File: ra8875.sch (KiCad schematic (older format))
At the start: 6 parts

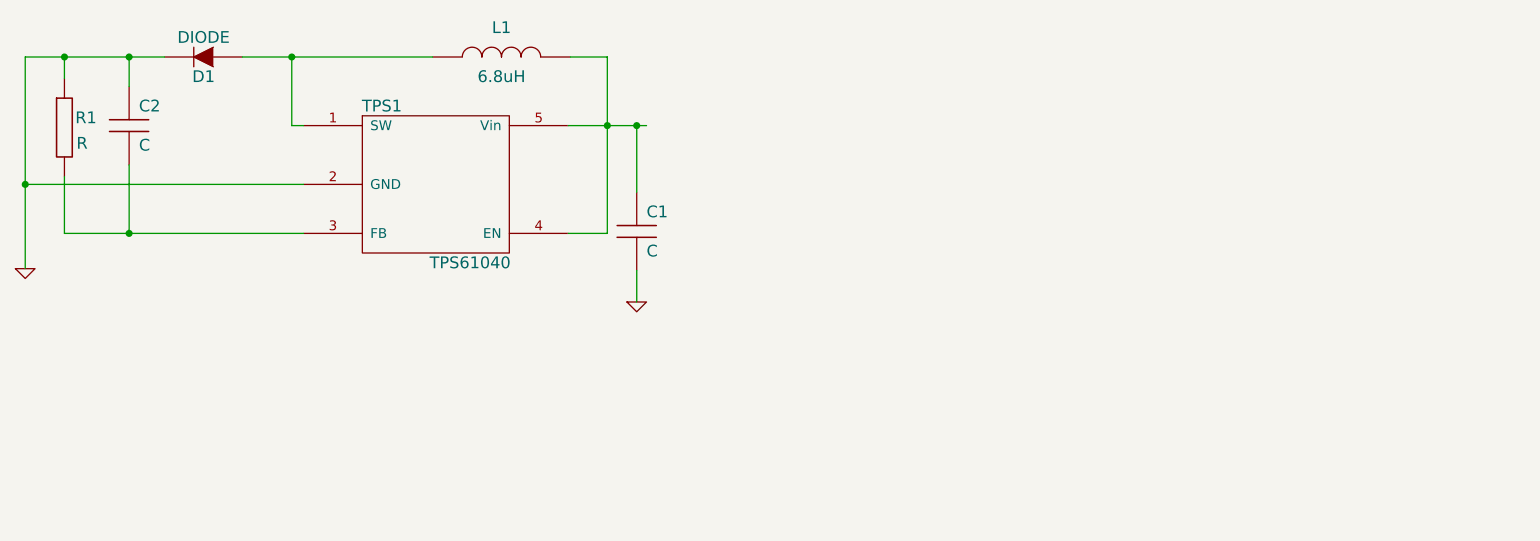
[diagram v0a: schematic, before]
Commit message: Add datasheets, appnotes and also completes the preliminary design for the TPS61040 power supply for the LCD backlight
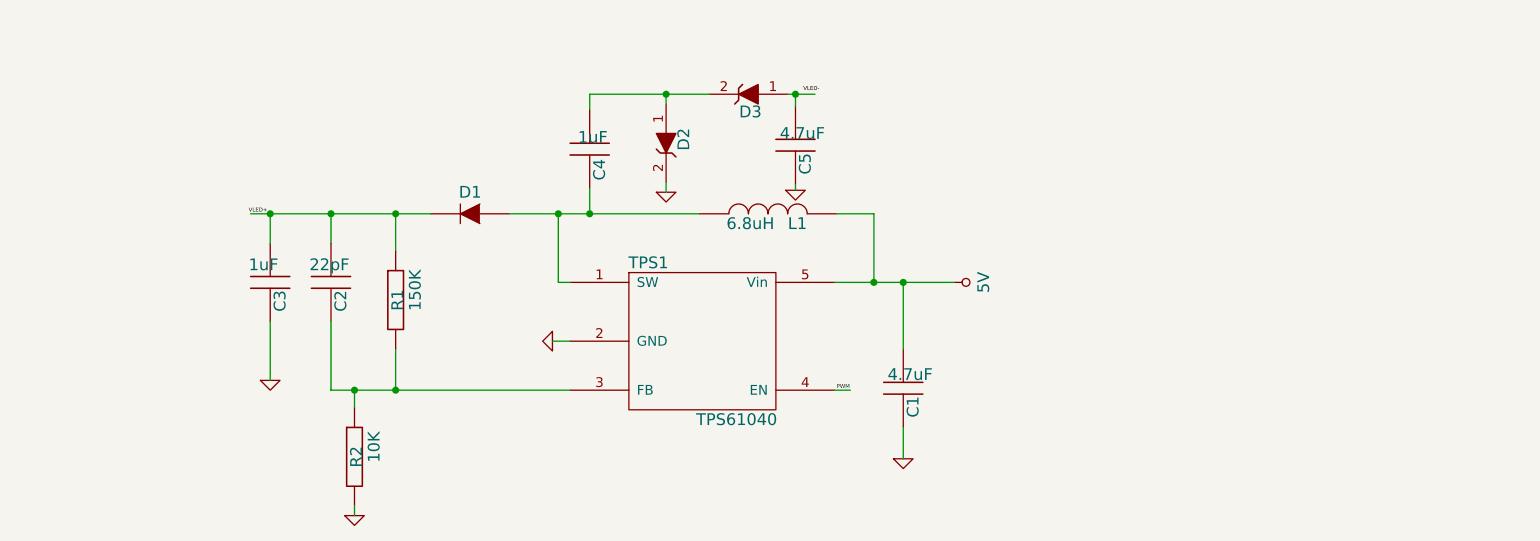
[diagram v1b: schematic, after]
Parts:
- added C3, C4: 1uF, symbol C
- added C5: 4.7uF, symbol C
- added D2, D3: ZENER, symbol ZENER
- added R2: 10K, symbol R
- C1: value C -> 4.7uF
- C2: value C -> 22pF
- R1: value R -> 150K
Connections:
- net labels added: 5V, PWM, VLED+, VLED-
- wire segments 18 -> 28
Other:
- moved on the sheet: C1, C2, D1, L1, R1, TPS1

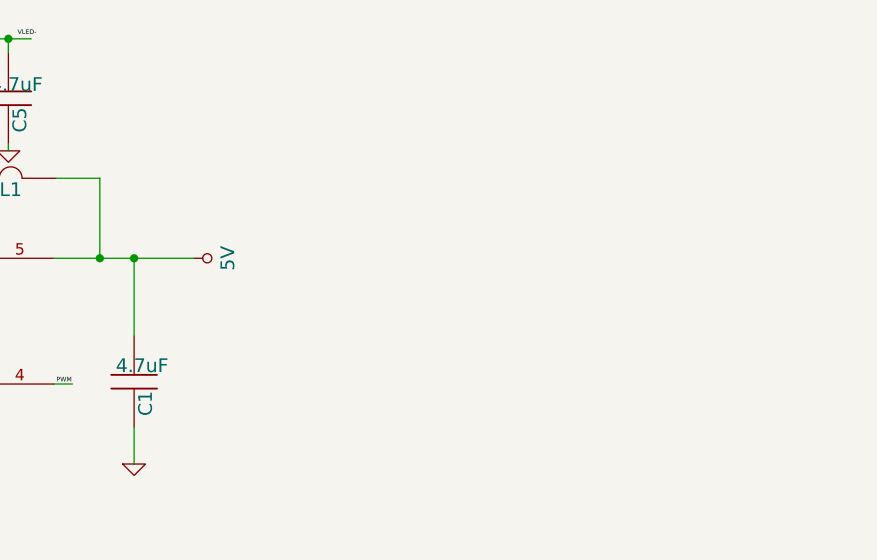
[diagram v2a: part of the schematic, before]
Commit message: Added Micrel 3.3v component
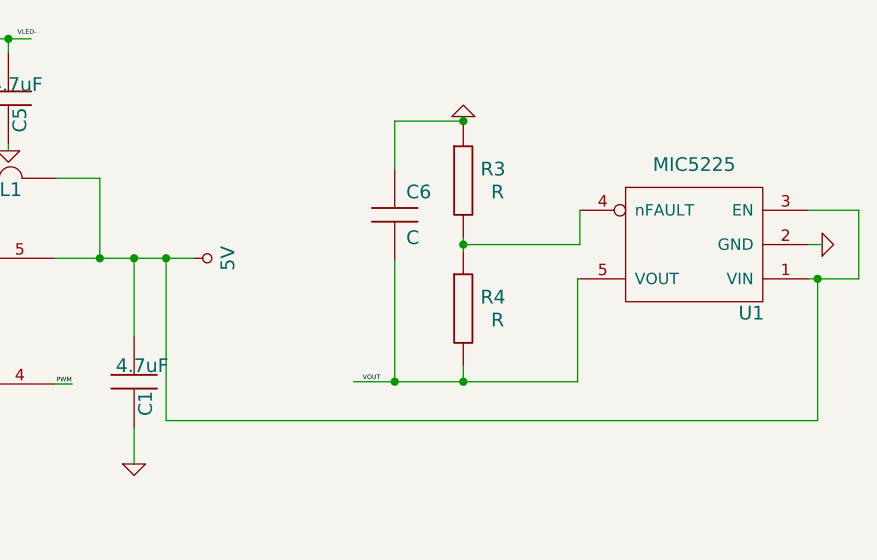
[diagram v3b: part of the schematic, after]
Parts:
- added C6: C, symbol C
- added R3, R4: R, symbol R
- added U1: MIC5225, symbol MIC2090-1YM5
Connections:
- net labels added: VOUT
- wire segments 28 -> 46
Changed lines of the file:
@@
 Sheet 1 1
 Title ""
-Date "7 may 2014"
+Date "20 may 2014"
 Rev ""
 Comp ""
@@
 	1    0    0    -1
 $EndComp
-Wire Wire Line
-	4980 2340 5590 2340
-Wire Wire Line
-	5330 2340 5330 2680
-Connection ~ 5330 2340
-Wire Wire Line
-	5330 3080 5330 3240
-Wire Wire Line
-	4990 1990 5180 1990
-Wire Wire Line
-	3320 1990 4290 1990
-Wire Wire Line
-	3630 2340 3570 2340
-Wire Wire Line
-	3570 2340 3570 1990
-Connection ~ 3570 1990
-Wire Wire Line
-	2000 1990 2920 1990
-Wire Wire Line
-	2410 2890 3630 2890
-Wire Wire Line
-	2740 1990 2740 2180
-Connection ~ 2740 1990
-Wire Wire Line
-	2410 2540 2410 2890
-Wire Wire Line
-	2410 1990 2410 2140
-Connection ~ 2410 1990
-Wire Wire Line
-	2530 2890 2530 2980
-Connection ~ 2530 2890
 $Comp
 L R R2
@@
 	1    0    0    -1
 $EndComp
-Wire Wire Line
-	2530 3480 2530 3530
-Wire Wire Line
-	2740 2680 2740 2890
-Connection ~ 2740 2890
 $Comp
 L GND #PWR04
@@
 	0    1    1    0
 $EndComp
-Wire Wire Line
-	3630 2640 3540 2640
 $Comp
 L C C3
@@
 	1    0    0    -1
 $EndComp
-Wire Wire Line
-	2100 1990 2100 2140
-Connection ~ 2100 1990
-Wire Wire Line
-	2100 2540 2100 2840
-Wire Wire Line
-	3730 1860 3730 1990
-Connection ~ 3730 1990
 $Comp
 L C C4
@@
 	1    0    0    -1
 $EndComp
-Wire Wire Line
-	3730 1460 3730 1380
-Wire Wire Line
-	3730 1380 4340 1380
-Wire Wire Line
-	4120 1380 4120 1430
 $Comp
 L GND #PWR05
@@
 	0    1    1    0
 $EndComp
-Wire Wire Line
-	4120 1830 4120 1880
-Connection ~ 4120 1380
 $Comp
 L ZENER D3
@@
 	-1   0    0    1
 $EndComp
-Wire Wire Line
-	4740 1380 4880 1380
-Wire Wire Line
-	4780 1380 4780 1440
-Connection ~ 4780 1380
 $Comp
 L C C5
@@
 	1    0    0    -1
 $EndComp
-Wire Wire Line
-	4780 1840 4780 1870
 $Comp
 L GND #PWR06
@@
 $EndComp
 $Comp
-L 5V #PWR?
+L 5V #PWR07
 U 1 1 535AA5B6
 P 5590 2340
-F 0 "#PWR?" H 5590 2300 30  0001 C CNN
+F 0 "#PWR07" H 5590 2300 30  0001 C CNN
 F 1 "5V" H 5590 2490 60  0000 C CNN
 F 2 "" H 5590 2340 60  0000 C CNN
@@
 	0    1    1    0
 $EndComp
-Wire Wire Line
-	5180 1990 5180 2340
-Connection ~ 5180 2340
-Wire Wire Line
-	4980 2890 5060 2890
 Text Label 4990 2890 0    20   ~ 0
 PWM
@@
 Text Label 1990 1990 0    20   ~ 0
 VLED+
+Wire Wire Line
+	4980 2340 5590 2340
+Wire Wire Line
+	5330 2340 5330 2680
+Connection ~ 5330 2340
+Wire Wire Line
+	5330 3080 5330 3240
+Wire Wire Line
+	4990 1990 5180 1990
+Wire Wire Line
+	3320 1990 4290 1990
+Wire Wire Line
+	3630 2340 3570 2340
+Wire Wire Line
+	3570 2340 3570 1990
+Connection ~ 3570 1990
+Wire Wire Line
+	2000 1990 2920 1990
+Wire Wire Line
+	2410 2890 3630 2890
+Wire Wire Line
+	2740 1990 2740 2180
+Connection ~ 2740 1990
+Wire Wire Line
+	2410 2540 2410 2890
+Wire Wire Line
+	2410 1990 2410 2140
+Connection ~ 2410 1990
+Wire Wire Line
+	2530 2890 2530 2980
+Connection ~ 2530 2890
+Wire Wire Line
+	2530 3480 2530 3530
+Wire Wire Line
+	2740 2680 2740 2890
+Connection ~ 2740 2890
+Wire Wire Line
+	3630 2640 3540 2640
+Wire Wire Line
+	2100 1990 2100 2140
+Connection ~ 2100 1990
+Wire Wire Line
+	2100 2540 2100 2840
+Wire Wire Line
+	3730 1860 3730 1990
+Connection ~ 3730 1990
+Wire Wire Line
+	3730 1460 3730 1380
+Wire Wire Line
+	3730 1380 4340 1380
+Wire Wire Line
+	4120 1380 4120 1430
+Wire Wire Line
+	4120 1830 4120 1880
+Connection ~ 4120 1380
+Wire Wire Line
+	4740 1380 4880 1380
+Wire Wire Line
+	4780 1380 4780 1440
+Connection ~ 4780 1380
+Wire Wire Line
+	4780 1840 4780 1870
+Wire Wire Line
+	5180 1990 5180 2340
+Connection ~ 5180 2340
+Wire Wire Line
+	4980 2890 5060 2890
+$Comp
+L MIC2090-1YM5 U1
+U 1 1 537B56B1
+P 7780 2180
+F 0 "U1" H 7530 2580 60  0000 C CNN
+F 1 "MIC5225" H 7780 1930 60  0000 C CNN
+F 2 "" H 7780 2180 60  0000 C CNN
+F 3 "" H 7780 2180 60  0000 C CNN
+	1    7780 2180
+	-1   0    0    1
+$EndComp
+Wire Wire Line
+	5470 2340 5470 3050
+Wire Wire Line
+	5470 3050 8320 3050
+Wire Wire Line
+	8320 3050 8320 2430
+Connection ~ 5470 2340
+Wire Wire Line
+	8280 2430 8500 2430
+$Comp
+L R R3
+U 1 1 537B66B9
+P 6770 2000
+F 0 "R3" H 6900 2050 60  0000 C CNN
+F 1 "R" H 6920 1950 60  0000 C CNN
+F 2 "" H 6770 2000 60  0000 C CNN
+F 3 "" H 6770 2000 60  0000 C CNN
+	1    6770 2000
+	1    0    0    -1
+$EndComp
+$Comp
+L R R4
+U 1 1 537B66D0
+P 6770 2560
+F 0 "R4" H 6900 2610 60  0000 C CNN
+F 1 "R" H 6920 2510 60  0000 C CNN
+F 2 "" H 6770 2560 60  0000 C CNN
+F 3 "" H 6770 2560 60  0000 C CNN
+	1    6770 2560
+	1    0    0    -1
+$EndComp
+Wire Wire Line
+	6770 2250 6770 2310
+Wire Wire Line
+	7270 2880 7270 2430
+Wire Wire Line
+	7280 2130 7280 2280
+Wire Wire Line
+	7280 2280 6770 2280
+Connection ~ 6770 2280
+Wire Wire Line
+	6770 1750 6770 1720
+$Comp
+L GND #PWR08
+U 1 1 537B679E
+P 6770 1720
+F 0 "#PWR08" H 6770 1720 30  0001 C CNN
+F 1 "GND" H 6770 1650 30  0001 C CNN
+F 2 "" H 6770 1720 60  0000 C CNN
+F 3 "" H 6770 1720 60  0000 C CNN
+	1    6770 1720
+	-1   0    0    1
+$EndComp
+Wire Wire Line
+	6770 2810 6770 2880
+Wire Wire Line
+	6290 2880 7270 2880
+$Comp
+L C C6
+U 1 1 537B6930
+P 6470 2150
+F 0 "C6" H 6520 2250 60  0000 L CNN
+F 1 "C" H 6520 2050 60  0000 L CNN
+F 2 "" H 6470 2150 60  0000 C CNN
+F 3 "" H 6470 2150 60  0000 C CNN
+	1    6470 2150
+	1    0    0    -1
+$EndComp
+Wire Wire Line
+	6770 1740 6470 1740
+Connection ~ 6770 1740
+Wire Wire Line
+	6470 2880 6470 2350
+Connection ~ 6770 2880
+Wire Wire Line
+	8280 2280 8340 2280
+$Comp
+L GND #PWR09
+U 1 1 537B6C18
+P 8340 2280
+F 0 "#PWR09" H 8340 2280 30  0001 C CNN
+F 1 "GND" H 8340 2210 30  0001 C CNN
+F 2 "" H 8340 2280 60  0000 C CNN
+F 3 "" H 8340 2280 60  0000 C CNN
+	1    8340 2280
+	0    -1   -1   0
+$EndComp
+Wire Wire Line
+	8500 2430 8500 2130
+Wire Wire Line
+	8500 2130 8280 2130
+Connection ~ 8320 2430
+Wire Wire Line
+	7270 2430 7280 2430
+Wire Wire Line
+	6470 1740 6470 1950
+Connection ~ 6470 2880
+Text Label 6330 2880 0    20   ~ 0
+VOUT
 $EndSCHEMATC

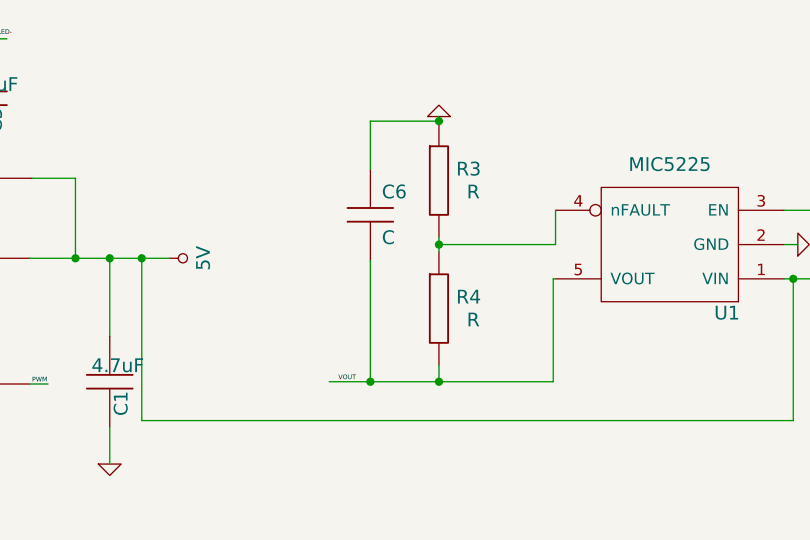
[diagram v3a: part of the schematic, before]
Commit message: Modify layout to reduce the amount of copper pour and also component placement to make it easier to solder
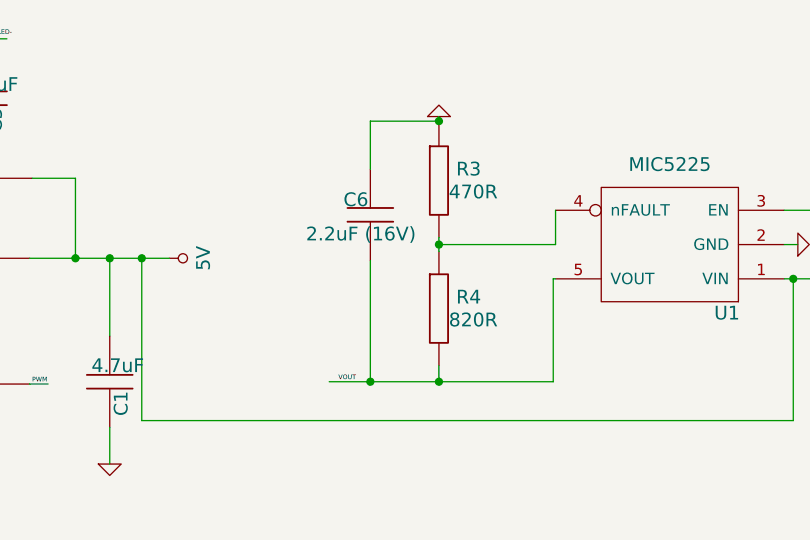
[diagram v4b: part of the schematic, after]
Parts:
- C6: value C -> 2.2uF (16V)
- R3: value R -> 470R
- R4: value R -> 820R
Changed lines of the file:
@@
 Sheet 1 1
 Title ""
-Date "20 may 2014"
+Date "1 jun 2014"
 Rev ""
 Comp ""
@@
 P 6770 2000
 F 0 "R3" H 6900 2050 60  0000 C CNN
-F 1 "R" H 6920 1950 60  0000 C CNN
+F 1 "470R" H 6920 1950 60  0000 C CNN
 F 2 "" H 6770 2000 60  0000 C CNN
 F 3 "" H 6770 2000 60  0000 C CNN
@@
 P 6770 2560
 F 0 "R4" H 6900 2610 60  0000 C CNN
-F 1 "R" H 6920 2510 60  0000 C CNN
+F 1 "820R" H 6920 2510 60  0000 C CNN
 F 2 "" H 6770 2560 60  0000 C CNN
 F 3 "" H 6770 2560 60  0000 C CNN
@@
 U 1 1 537B6930
 P 6470 2150
-F 0 "C6" H 6520 2250 60  0000 L CNN
-F 1 "C" H 6520 2050 60  0000 L CNN
+F 0 "C6" H 6352 2216 60  0000 L CNN
+F 1 "2.2uF (16V)" H 6188 2066 60  0000 L CNN
 F 2 "" H 6470 2150 60  0000 C CNN
 F 3 "" H 6470 2150 60  0000 C CNN
